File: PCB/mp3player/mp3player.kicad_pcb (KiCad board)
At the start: 2 copper layers, 60 x 85.5 mm, 70 parts, among them J1 AudioJack3, J2 Battery, J3 USB_C, J4 Micro_SD_Card, J5 TFT SPI, SW1 Play, SW10 Power_sw, SW11 Next, SW12 Prev, SW2 Trk Prev, SW3 Trk Next, SW4 Mode Prev, SW5 Mode Next, SW6 Eq, SW7 Power, SW8 RESET, SW9 BOOT, U1 ESP32-S3-WROOM-1, U2 ES8388, U3 AP2112K-3.3, U4 MCP73831-2-OT, U5 USBLC6-2SC6

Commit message: cont.
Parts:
- R10, R11, R12, R13: value R -> 33
- moved R13 90.0 mm to (241.5, 98.0), turned to 0 degrees
- moved R10 90.0 mm to (241.5, 93.5), turned to 0 degrees
- moved R12 90.0 mm to (241.5, 96.5), turned to 0 degrees
- moved R11 90.0 mm to (241.5, 95.0), turned to 0 degrees
- moved U3 64.5 mm to (198.0, 94.5)
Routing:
- net /CODEC_MCLK: track 0.00 -> 25.6 mm
- net /CODEC_BCLK: track 0.00 -> 22.7 mm, vias 0 -> 2
- net /CODEC_LRCK: track 0.00 -> 19.6 mm
- net /CODEC_DIN: track 0.00 -> 18.8 mm
- net VSW: track 0.00 -> 7.33 mm
- net /12S_DOUT: track 0.00 -> 1.95 mm
- net /12S_MCLK: track 0.00 -> 1.89 mm
- net /12S_LRCK: track 0.00 -> 1.85 mm
- net /12S_BCLK: track 0.00 -> 1.79 mm

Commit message: cont.
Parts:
- C1, R7: moved to F.Cu
- moved R3 96.9 mm to (243.8, 108.7), turned to -90 degrees
- moved R4 95.2 mm to (242.2, 108.7), turned to -90 degrees
- moved R7 88.6 mm to (235.5, 112.9), turned to -90 degrees
- moved C22 63.4 mm to (201.8, 95.5)
- moved C17 62.5 mm to (201.8, 93.5)
- moved C1 59.4 mm to (198.2, 91.8)
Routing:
- net GND: track 5.87 -> 17.9 mm, vias 0 -> 1
- net +3V3: track 24.8 -> 32.7 mm, vias 0 -> 1
- net VDD_CODEC: track 0.00 -> 7.53 mm, vias 0 -> 2
- net HPVDD: track 0.46 -> 4.59 mm, vias 0 -> 2
- net AU_GND: track 7.91 -> 10.4 mm, vias 0 -> 1
- net /LOUT1: track 14.1 -> 14.7 mm
- net /ROUT1: track 22.8 -> 23.5 mm

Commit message: cont.
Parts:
- moved C18 103.4 mm to (231.2, 144.2), turned to 0 degrees
- moved C2 98.3 mm to (241.8, 85.5), turned to 90 degrees
- moved C19 86.3 mm to (201.8, 159.5)
- moved C15 62.9 mm to (201.8, 97.5), turned to 0 degrees
- moved C21 47.6 mm to (192.8, 104.4), turned to 0 degrees
- moved C12 4.76 mm to (147.5, 99.8)
- moved C3 2.00 mm to (143.5, 85.2)
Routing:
- net +3V3: track 32.7 -> 55.4 mm, vias 1 -> 2
- net GND: track 17.9 -> 36.5 mm, vias 1 -> 2
- net VBUS: track 45.7 -> 57.4 mm, vias 1 -> 2
- net VSW: track 7.33 -> 12.1 mm, vias 0 -> 1
- net /CC1: track 5.46 -> 4.57 mm, vias 1 -> 2

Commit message: cont.
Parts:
- C19, C20, C3, C4, C5: moved to F.Cu
- moved C4 99.2 mm to (240.0, 112.8), turned to 0 degrees
- moved C5 99.1 mm to (240.0, 114.8)
- moved C3 87.5 mm to (231.0, 86.2), turned to -90 degrees
- moved C20 74.8 mm to (190.2, 157.8), turned to 0 degrees
- moved C6 18.7 mm to (140.5, 113.2)
- moved C19 9.58 mm to (204.2, 150.2), turned to 90 degrees
- moved C14 8.01 mm to (152.5, 111.0)
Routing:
- net VDD_CODEC: track 7.53 -> 15.7 mm, vias 2 -> 3
- net AU_GND: track 10.4 -> 12.6 mm, vias 1 -> 3
- net VBAT: track 69.5 -> 71.7 mm
- net /EN: track 53.3 -> 55.1 mm, vias 2 -> 3
- net VBUS: track 57.4 -> 58.5 mm

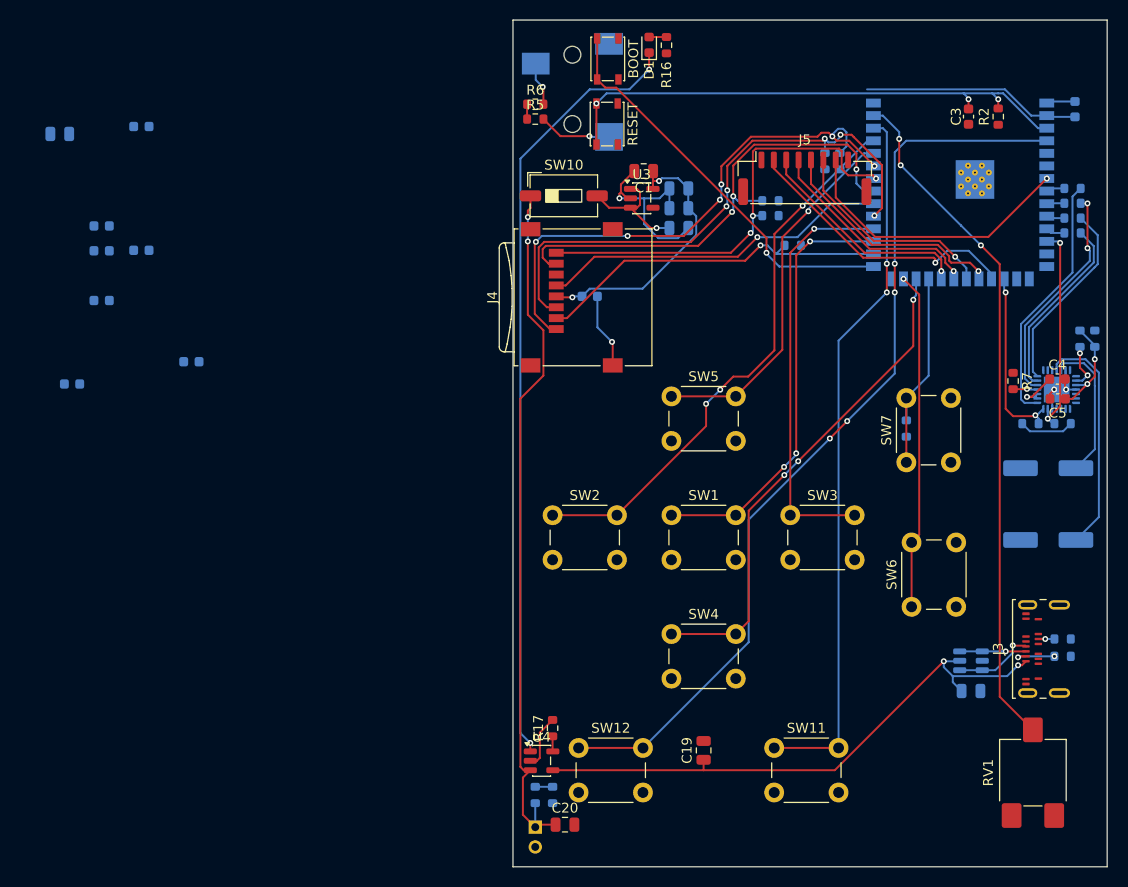
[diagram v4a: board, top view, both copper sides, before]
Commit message: all parts placed
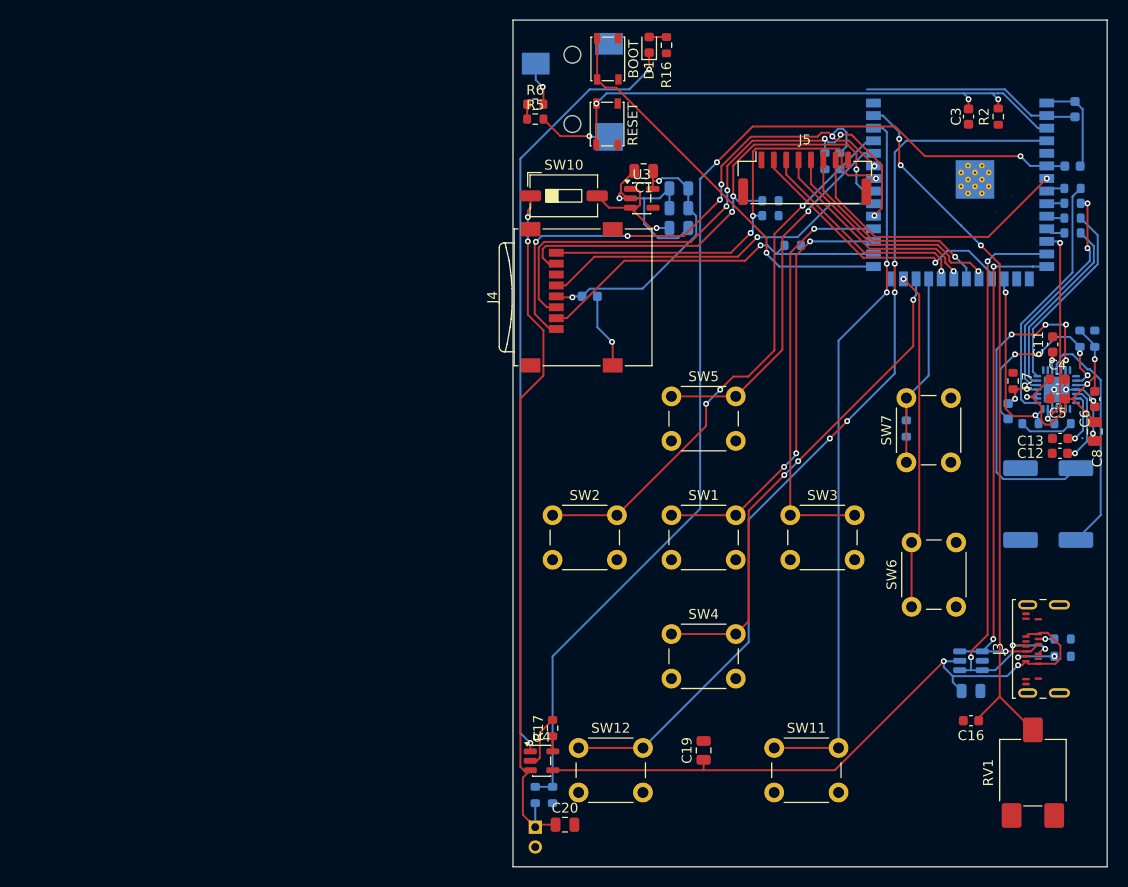
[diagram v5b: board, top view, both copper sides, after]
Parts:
- C11, C12, C13, C16, C6, C8: moved to F.Cu
- moved C8 108.7 mm to (243.8, 118.0), turned to -90 degrees
- moved C6 103.3 mm to (243.8, 114.8), turned to -90 degrees
- moved C16 103.0 mm to (231.2, 147.2)
- moved C13 97.8 mm to (240.2, 118.8)
- moved C11 96.5 mm to (239.5, 109.2), turned to 90 degrees
- moved C12 95.0 mm to (240.2, 120.2)
- moved C7 93.4 mm to (235.0, 116.0), turned to 90 degrees
- moved C14 91.1 mm to (241.5, 91.2), turned to 0 degrees
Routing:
- net /VBAT_SENSE: track 1.75 -> 110.0 mm, vias 0 -> 2
- net /USB_DM: track 8.19 -> 60.8 mm, vias 1 -> 4
- net /USB_DP: track 6.69 -> 53.0 mm, vias 1 -> 3
- net /LOUT1: track 14.7 -> 34.1 mm, vias 0 -> 4
- net HPVDD: track 4.59 -> 19.9 mm, vias 2 -> 4
- net VDD_CODEC: track 15.7 -> 27.6 mm
- net AU_GND: track 12.6 -> 21.9 mm, vias 3 -> 6
- net VBUS: track 58.5 -> 67.7 mm
- net /ADCVREF: track 0.00 -> 8.05 mm, vias 0 -> 1
- net GND: track 36.5 -> 43.5 mm
- net /VMID: track 0.00 -> 5.74 mm, vias 0 -> 1
- net /SLIDE_POT: track 69.3 -> 72.6 mm
- net /VREF: track 0.00 -> 1.86 mm, vias 0 -> 1

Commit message: audio gnd fully routed
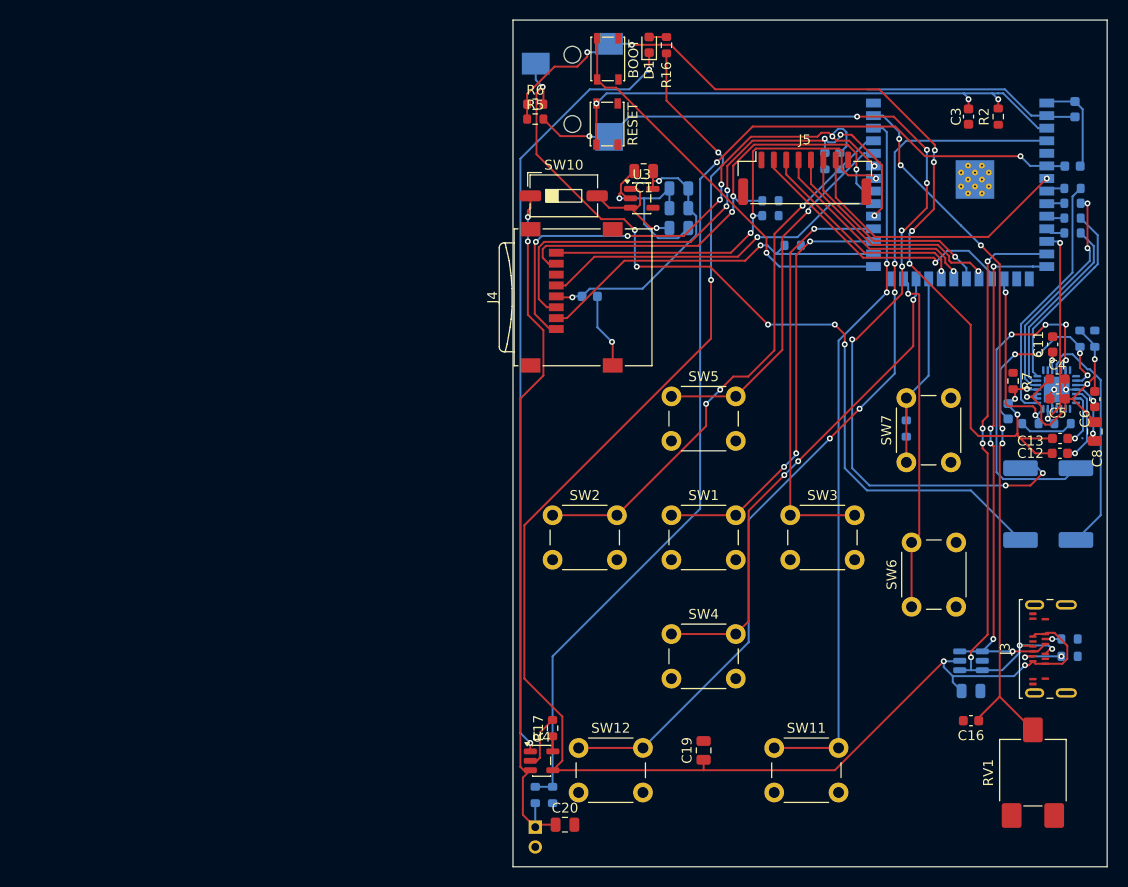
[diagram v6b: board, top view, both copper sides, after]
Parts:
- moved J3 0.70 mm to (240.7, 140.0)
- moved R18 0.70 mm to (241.2, 140.8)
- moved R19 0.70 mm to (241.2, 139.0)
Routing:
- net AU_GND: track 21.9 -> 119.6 mm, vias 6 -> 13
- net /HP_L: track 7.37 -> 100.4 mm, vias 1 -> 9
- net VBUS: track 67.7 -> 153.5 mm, vias 2 -> 4
- net /HP_R: track 4.42 -> 86.4 mm, vias 1 -> 6
- net /USB_DM: track 60.8 -> 61.9 mm, vias 4 -> 6
- net /USB_DP: track 53.0 -> 54.0 mm, vias 3 -> 5
- net /BTN_EQ: track 34.1 -> 34.7 mm
- net /SLIDE_POT: track 72.6 -> 72.8 mm, vias 3 -> 5

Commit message: cont.
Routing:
- net +3V3: track 55.4 -> 105.7 mm, vias 2 -> 7
- net /BTN_TRK_PREV: track 56.3 -> 69.3 mm, vias 3 -> 7
- net /BTN_MODE_NEXT: track 37.4 -> 47.8 mm, vias 1 -> 7
- net /SD_CMD: track 57.8 -> 63.5 mm, vias 5 -> 6
- net /NEXT: track 72.2 -> 73.1 mm, vias 2 -> 6
- net /PREV: track 93.0 -> 93.2 mm, vias 4 -> 6

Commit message: 3V3 net routing done :)
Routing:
- net +3V3: track 105.7 -> 203.9 mm, vias 7 -> 13
- net /NEXT: track 73.1 -> 73.4 mm, vias 6 -> 8
- net /EN: track 55.1 -> 55.2 mm, vias 3 -> 5
